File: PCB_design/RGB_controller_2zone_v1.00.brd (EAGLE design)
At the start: 75.9 x 64.8 mm, 24 parts, among them Q1 IRF512, Q2 IRF512, Q3 IRF512, Q4 IRF512, Q5 IRF512, Q6 IRF512

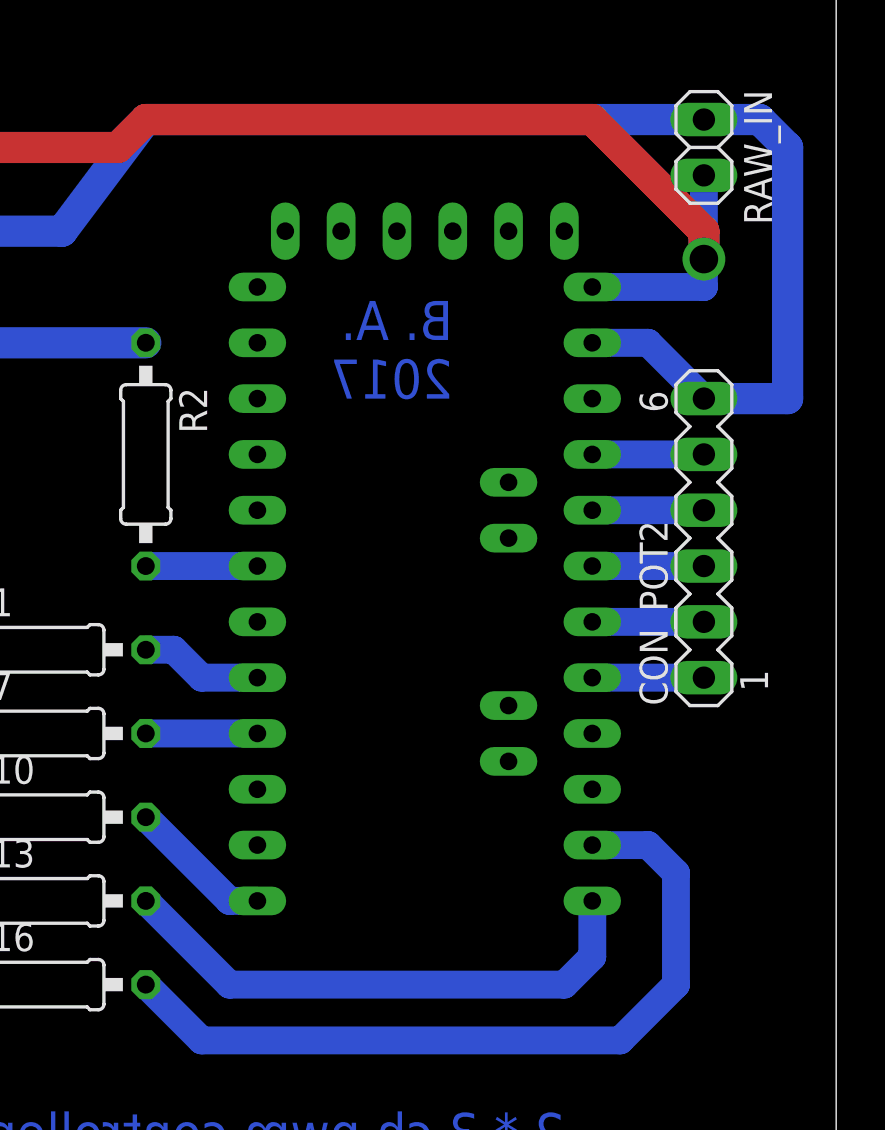
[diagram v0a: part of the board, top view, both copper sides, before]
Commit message: Change arduino layout to fit to the buyable clone
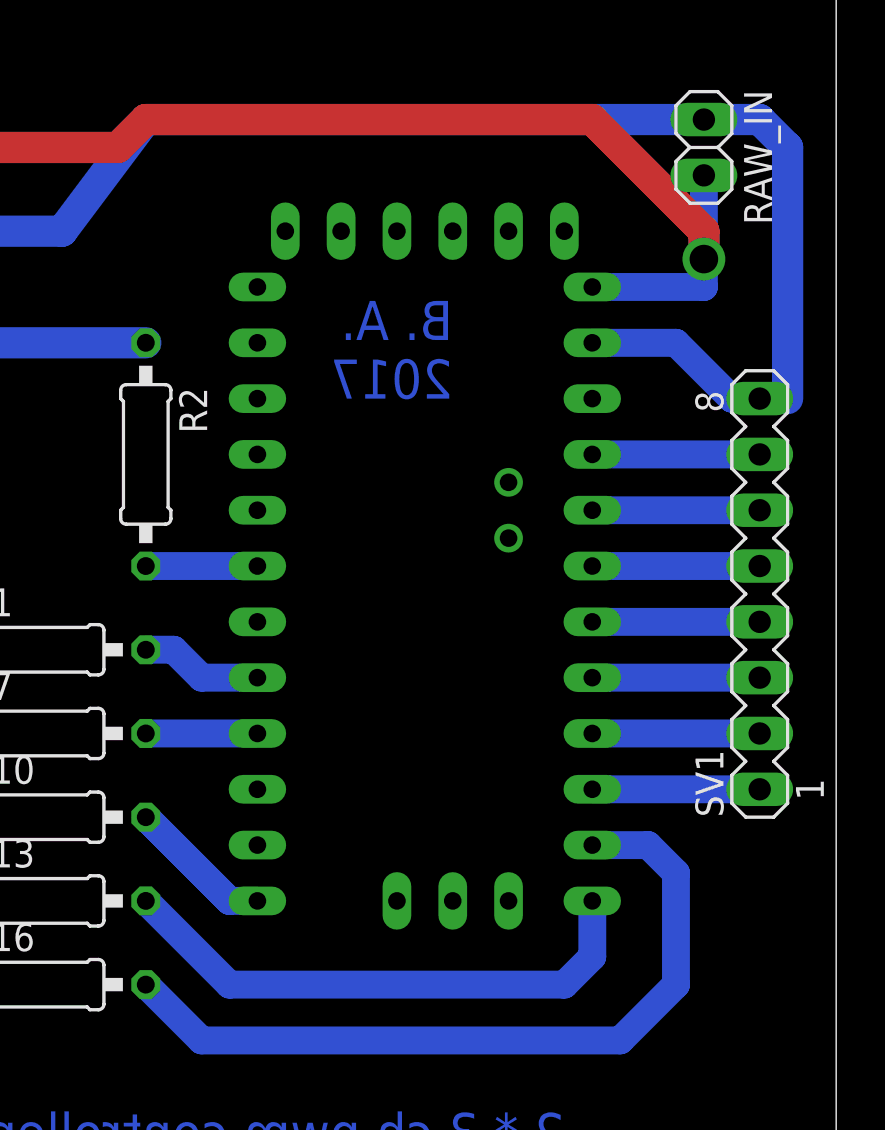
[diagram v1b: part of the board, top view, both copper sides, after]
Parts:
- removed CON_POT2: (no value), con-lstb:MA06-1
- added SV1: (no value), con-lstb:MA08-1
- U$1: value PRO-MINI-2 -> ABK-PRO-MINI; device Arduino-clone:PRO-MINI-2 -> Arduino-clone:ABK-PRO-MINI
- moved U$1 7.41 mm to (54.6, 43.2)
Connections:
- new net D12: SV1.1, U$1.D12
- new net D13: SV1.2, U$1.D13
- net A0: now also SV1.6; no longer CON_POT2.4
- net A1: now also SV1.5; no longer CON_POT2.3
- net A2: now also SV1.4; no longer CON_POT2.2
- net A3: now also SV1.3; no longer CON_POT2.1
- net GND: now also SV1.8; no longer CON_POT2.6
- net VCC: now also SV1.7; no longer CON_POT2.5
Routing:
- net D13: track 0.00 -> 7.62 mm
- net D12: track 0.00 -> 7.62 mm
- net IC_PWM_OUT_3: track 6.66 -> 12.0 mm
- net VCC: track 5.08 -> 7.62 mm
- net A3: track 5.08 -> 7.62 mm
- net A2: track 5.08 -> 7.62 mm
- net A1: track 5.08 -> 7.62 mm
- net A0: track 5.08 -> 7.62 mm
- net GND: track 165.8 -> 167.1 mm
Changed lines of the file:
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@@
 </element>
 <element name="RAW_IN" library="pinhead" package="1X02" value="" x="69.85" y="55.88" rot="R270"/>
-<element name="U$1" library="Arduino-clone" package="PRO-MINI-2" value="PRO-MINI-2" x="58.42" y="36.83"/>
-<element name="CON_POT2" library="con-lstb" package="MA06-1" value="" x="69.85" y="38.1" rot="R90">
-<attribute name="MF" value="" x="69.85" y="38.1" size="1.778" layer="27" rot="R90" display="off"/>
-<attribute name="MPN" value="" x="69.85" y="38.1" size="1.778" layer="27" rot="R90" display="off"/>
-<attribute name="OC_FARNELL" value="unknown" x="69.85" y="38.1" size="1.778" layer="27" rot="R90" display="off"/>
-<attribute name="OC_NEWARK" value="unknown" x="69.85" y="38.1" size="1.778" layer="27" rot="R90" display="off"/>
-</element>
 <element name="R3" library="rcl" package="0207/10" value="10k" x="24.13" y="50.8"/>
 <element name="R4" library="rcl" package="0207/10" value="10k" x="24.13" y="41.91"/>
@@
 <element name="R8" library="rcl" package="0207/10" value="10k" x="24.13" y="15.24"/>
 <element name="R9" library="rcl" package="0207/10" value="10k" x="24.13" y="6.35"/>
+<element name="U$1" library="Arduino-clone" package="ABK-PRO-MINI" value="ABK-PRO-MINI" x="54.61" y="43.18"/>
+<element name="SV1" library="con-lstb" package="MA08-1" value="" x="72.39" y="35.56" rot="R90">
+<attribute name="MF" value="" x="72.39" y="35.56" size="1.778" layer="27" rot="R90" display="off"/>
+<attribute name="MPN" value="" x="72.39" y="35.56" size="1.778" layer="27" rot="R90" display="off"/>
+<attribute name="OC_FARNELL" value="unknown" x="72.39" y="35.56" size="1.778" layer="27" rot="R90" display="off"/>
+<attribute name="OC_NEWARK" value="unknown" x="72.39" y="35.56" size="1.778" layer="27" rot="R90" display="off"/>
+</element>
 </elements>
 <signals>
@@
 <contactref element="RAW" pad="1"/>
 <contactref element="RAW_IN" pad="1"/>
-<contactref element="U$1" pad="GND"/>
-<contactref element="CON_POT2" pad="6"/>
 <contactref element="Q1" pad="S"/>
 <contactref element="R3" pad="1"/>
@@
 <wire x1="44.45" y1="57.15" x2="72.39" y2="57.15" width="1.4224" layer="16"/>
 <wire x1="72.39" y1="57.15" x2="73.66" y2="55.88" width="1.4224" layer="16"/>
-<wire x1="73.66" y1="55.88" x2="73.66" y2="44.45" width="1.4224" layer="16"/>
-<wire x1="69.85" y1="44.45" x2="73.66" y2="44.45" width="1.4224" layer="16"/>
-<wire x1="64.77" y1="46.99" x2="67.31" y2="46.99" width="1.27" layer="16"/>
-<wire x1="67.31" y1="46.99" x2="69.85" y2="44.45" width="1.27" layer="16"/>
-<wire x1="73.66" y1="55.88" x2="69.85" y2="57.15" width="0" layer="19" extent="16-16"/>
+<wire x1="73.66" y1="44.45" x2="73.66" y2="55.88" width="1.4224" layer="16"/>
+<contactref element="U$1" pad="GND"/>
+<contactref element="SV1" pad="8"/>
+<wire x1="71.12" y1="44.45" x2="68.58" y2="46.99" width="1.27" layer="16"/>
+<wire x1="71.12" y1="44.45" x2="73.66" y2="44.45" width="1.27" layer="16"/>
+<wire x1="64.77" y1="46.99" x2="68.58" y2="46.99" width="1.27" layer="16"/>
+<wire x1="72.39" y1="44.45" x2="71.12" y2="44.45" width="1.27" layer="16"/>
+<wire x1="72.39" y1="57.15" x2="69.85" y2="57.15" width="0" layer="19" extent="16-16"/>
 </signal>
 <signal name="GATE_1">
@@
 <contactref element="U$1" pad="D5"/>
 <wire x1="44.45" y1="33.02" x2="45.72" y2="33.02" width="1.27" layer="16"/>
-<wire x1="45.72" y1="33.02" x2="46.99" y2="31.75" width="1.27" layer="16"/>
-<wire x1="46.99" y1="31.75" x2="49.53" y2="31.75" width="1.27" layer="16"/>
+<wire x1="46.99" y1="31.75" x2="45.72" y2="33.02" width="1.27" layer="16"/>
+<wire x1="49.53" y1="31.75" x2="46.99" y2="31.75" width="1.27" layer="16"/>
 </signal>
 <signal name="IC_PWM_OUT_2">
 <contactref element="R7" pad="2"/>
 <contactref element="U$1" pad="D6"/>
-<wire x1="44.45" y1="29.21" x2="49.53" y2="29.21" width="1.27" layer="16"/>
+<wire x1="49.53" y1="29.21" x2="44.45" y2="29.21" width="1.27" layer="16"/>
 </signal>
 <signal name="IC_PWM_OUT_3">
 <contactref element="R10" pad="2"/>
+<wire x1="44.45" y1="25.4" x2="48.26" y2="21.59" width="1.27" layer="16"/>
 <contactref element="U$1" pad="D9"/>
-<wire x1="44.45" y1="25.4" x2="48.26" y2="21.59" width="1.27" layer="16"/>
-<wire x1="48.26" y1="21.59" x2="49.53" y2="21.59" width="1.27" layer="16"/>
+<wire x1="49.53" y1="21.59" x2="48.26" y2="21.59" width="1.27" layer="16"/>
+<wire x1="48.26" y1="21.59" x2="44.45" y2="25.4" width="1.27" layer="16"/>
 </signal>
 <signal name="IC_PWM_OUT_4">
 <contactref element="R13" pad="2"/>
+<wire x1="48.26" y1="17.78" x2="63.5" y2="17.78" width="1.27" layer="16"/>
+<wire x1="64.77" y1="19.05" x2="63.5" y2="17.78" width="1.27" layer="16"/>
 <contactref element="U$1" pad="D10"/>
 <wire x1="44.45" y1="21.59" x2="48.26" y2="17.78" width="1.27" layer="16"/>
-<wire x1="48.26" y1="17.78" x2="63.5" y2="17.78" width="1.27" layer="16"/>
-<wire x1="63.5" y1="17.78" x2="64.77" y2="19.05" width="1.27" layer="16"/>
-<wire x1="64.77" y1="19.05" x2="64.77" y2="21.59" width="1.27" layer="16"/>
+<wire x1="64.77" y1="21.59" x2="64.77" y2="19.05" width="1.27" layer="16"/>
 </signal>
 <signal name="IC_PWM_OUT_5">
 <contactref element="R16" pad="2"/>
-<contactref element="U$1" pad="D11"/>
-<wire x1="64.77" y1="24.13" x2="67.31" y2="24.13" width="1.27" layer="16"/>
 <wire x1="67.31" y1="24.13" x2="68.58" y2="22.86" width="1.27" layer="16"/>
 <wire x1="68.58" y1="22.86" x2="68.58" y2="17.78" width="1.27" layer="16"/>
@@
 <wire x1="66.04" y1="15.24" x2="46.99" y2="15.24" width="1.27" layer="16"/>
 <wire x1="46.99" y1="15.24" x2="44.45" y2="17.78" width="1.27" layer="16"/>
+<contactref element="U$1" pad="D11"/>
+<wire x1="64.77" y1="24.13" x2="67.31" y2="24.13" width="1.27" layer="16"/>
 </signal>
 <signal name="+12V">
@@
 <contactref element="RAW" pad="2"/>
 <contactref element="RAW_IN" pad="2"/>
-<contactref element="U$1" pad="RAW"/>
-<wire x1="64.77" y1="49.53" x2="69.85" y2="49.53" width="1.27" layer="16"/>
 <wire x1="69.85" y1="49.53" x2="69.85" y2="50.8" width="1.27" layer="16"/>
 <wire x1="69.85" y1="50.8" x2="69.85" y2="54.61" width="1.27" layer="16"/>
@@
 <wire x1="69.85" y1="52.07" x2="69.85" y2="50.8" width="1.4224" layer="1"/>
 <via x="69.85" y="50.8" extent="1-16" drill="1.3" shape="square"/>
+<contactref element="U$1" pad="RAW"/>
+<wire x1="64.77" y1="49.53" x2="69.85" y2="49.53" width="1.27" layer="16"/>
 </signal>
 <signal name="A3">
 <contactref element="U$1" pad="A3"/>
-<contactref element="CON_POT2" pad="1"/>
-<wire x1="64.77" y1="31.75" x2="69.85" y2="31.75" width="1.27" layer="16"/>
+<contactref element="SV1" pad="3"/>
+<wire x1="64.77" y1="31.75" x2="72.39" y2="31.75" width="1.27" layer="16"/>
 </signal>
 <signal name="A2">
 <contactref element="U$1" pad="A2"/>
-<contactref element="CON_POT2" pad="2"/>
-<wire x1="64.77" y1="34.29" x2="69.85" y2="34.29" width="1.27" layer="16"/>
+<contactref element="SV1" pad="4"/>
+<wire x1="64.77" y1="34.29" x2="72.39" y2="34.29" width="1.27" layer="16"/>
 </signal>
 <signal name="A1">
 <contactref element="U$1" pad="A1"/>
-<contactref element="CON_POT2" pad="3"/>
-<wire x1="64.77" y1="36.83" x2="69.85" y2="36.83" width="1.27" layer="16"/>
+<contactref element="SV1" pad="5"/>
+<wire x1="64.77" y1="36.83" x2="72.39" y2="36.83" width="1.27" layer="16"/>
 </signal>
 <signal name="A0">
 <contactref element="U$1" pad="A0"/>
-<contactref element="CON_POT2" pad="4"/>
-<wire x1="64.77" y1="39.37" x2="69.85" y2="39.37" width="1.27" layer="16"/>
+<contactref element="SV1" pad="6"/>
+<wire x1="64.77" y1="39.37" x2="72.39" y2="39.37" width="1.27" layer="16"/>
 </signal>
 <signal name="VCC">
 <contactref element="U$1" pad="VCC"/>
-<contactref element="CON_POT2" pad="5"/>
-<wire x1="64.77" y1="41.91" x2="69.85" y2="41.91" width="1.27" layer="16"/>
+<contactref element="SV1" pad="7"/>
+<wire x1="72.39" y1="41.91" x2="64.77" y2="41.91" width="1.27" layer="16"/>
 </signal>
 <signal name="GATE_6">
@@
 <wire x1="31.75" y1="39.37" x2="27.94" y2="39.37" width="1.4224" layer="16"/>
 </signal>
+<signal name="D13">
+<contactref element="U$1" pad="D13"/>
+<contactref element="SV1" pad="2"/>
+<wire x1="64.77" y1="29.21" x2="72.39" y2="29.21" width="1.27" layer="16"/>
+</signal>
+<signal name="D12">
+<contactref element="U$1" pad="D12"/>
+<contactref element="SV1" pad="1"/>
+<wire x1="64.77" y1="26.67" x2="72.39" y2="26.67" width="1.27" layer="16"/>
+</signal>
 </signals>
